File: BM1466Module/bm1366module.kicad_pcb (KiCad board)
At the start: 4 copper layers, 50 x 50 mm, 38 parts, among them J2 Conn_02x10_Odd_Even, U1 25MHz, U2 BM1366_mode1

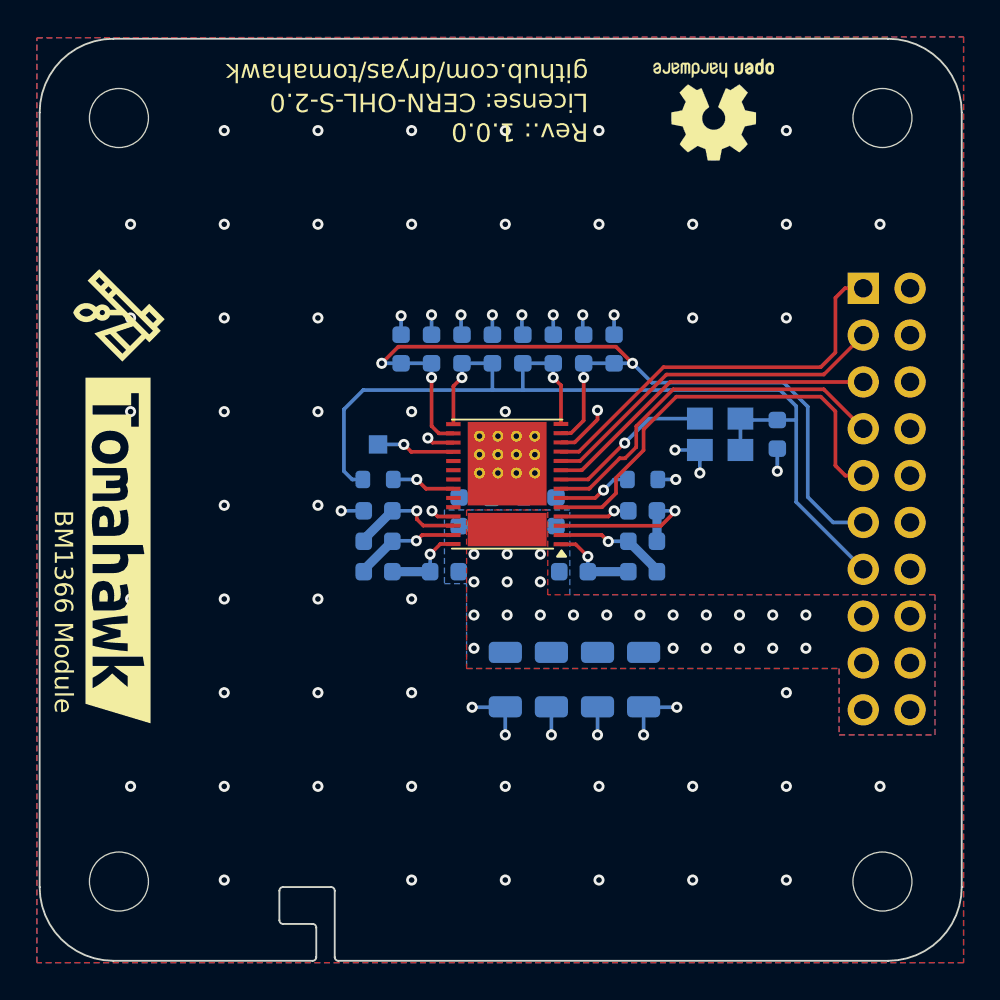
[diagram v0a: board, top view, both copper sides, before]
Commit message: Added support for TMP1075 temperature sensor to monitor ASIC
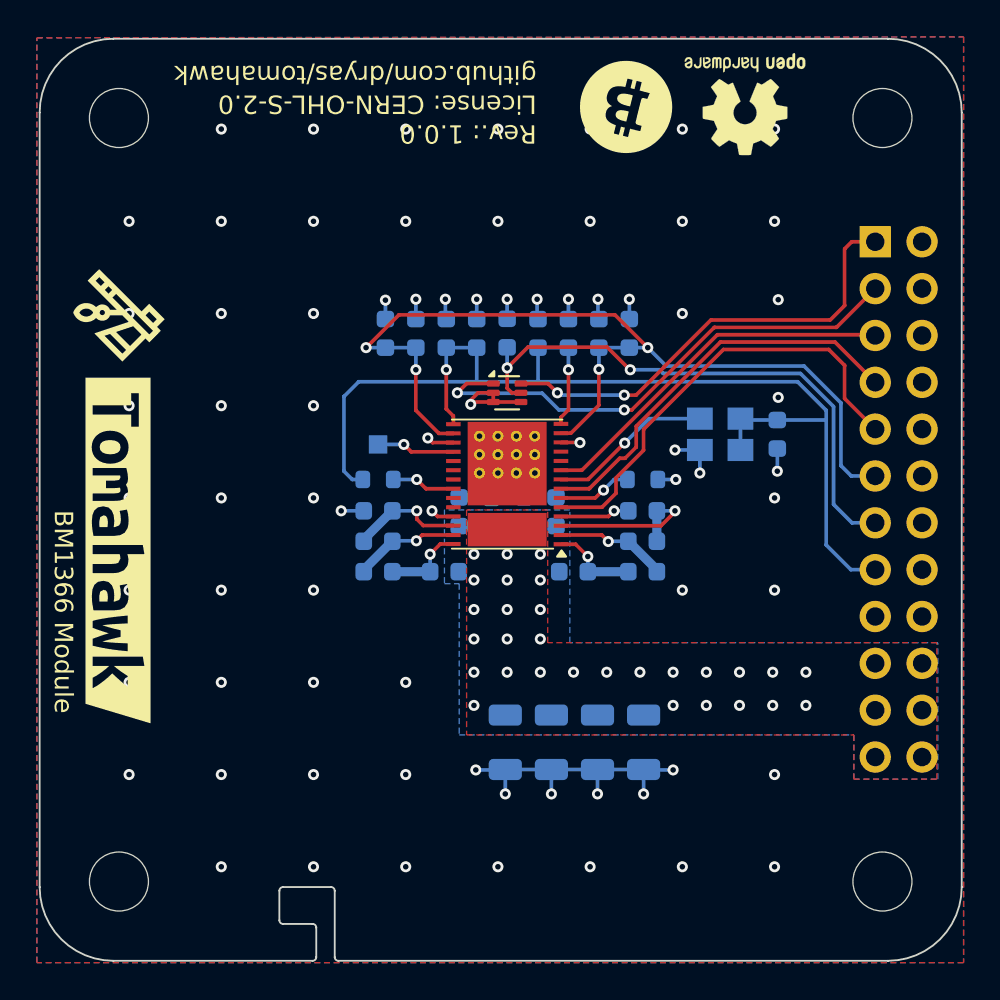
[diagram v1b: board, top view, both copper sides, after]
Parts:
- removed J2: Conn_02x10_Odd_Even, Connector_PinSocket_2.54mm:PinSocket_2x10_P2.54mm_Vertical
- added C13: 100nF, Capacitor_SMD:C_0603_1608Metric, B.Cu at (145.0, 86.2)
- added G***: LOGO, LOGO, F.Cu at (151.4, 74.0)
- added J1: Conn_02x12_Odd_Even, Connector_PinSocket_2.54mm:PinSocket_2x12_P2.54mm_Vertical, B.Cu at (165.0, 81.3)
- added U3: TMP1075, Package_TO_SOT_SMD:SOT-563, F.Cu at (145.0, 89.5)
- moved C2 3.40 mm to (152.4, 108.4)
- moved C3 3.40 mm to (149.9, 108.4)
- moved C4 3.40 mm to (147.4, 108.4)
- moved C5 3.40 mm to (144.9, 108.4)
- moved REF** 1.73 mm to (157.9, 73.8)
- moved C25 1.20 mm to (141.7, 86.2)
- moved C19 1.20 mm to (138.4, 86.2)
- moved C21 1.20 mm to (140.1, 86.2)
- moved C24 1.20 mm to (143.3, 86.2)
- moved C14 1.18 mm to (146.7, 86.2)
- moved C10 1.18 mm to (151.6, 86.2)
- moved C17 1.18 mm to (148.3, 86.2)
- moved C7 1.18 mm to (150.0, 86.2)
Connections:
- U2 pad 10: /TEMP_P -> unconnected-(U2-TEMP_P-Pad10)
- U2 pad 11: /TEMP_N -> unconnected-(U2-TEMP_N-Pad11)
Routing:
- net +3V3: track 0.00 -> 30.8 mm, vias 0 -> 2
- net /SCL: track 0.00 -> 27.9 mm, vias 0 -> 2
- net /SDA: track 0.00 -> 24.7 mm, vias 0 -> 2
- net /TEMP_N: track 21.8 -> 0.00 mm
- net /TEMP_P: track 19.2 -> 0.00 mm
- net GND: track 33.9 -> 44.2 mm, vias 76 -> 74
- net +1V8: track 58.1 -> 65.0 mm
- net +0V8: track 48.1 -> 51.2 mm
- net /CI: track 18.4 -> 20.1 mm
- net /RO: track 20.2 -> 21.9 mm
- net /RST_N: track 23.5 -> 24.6 mm
- net +1V2: track 0.00 -> 0.07 mm, vias 23 -> 29
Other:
- board text added: "+3,3V"
- board text added: "GND"
- board text added: "SCL"
- board text added: "SDA"
- board text removed: "Temp+"
- board text removed: "Temp-"
